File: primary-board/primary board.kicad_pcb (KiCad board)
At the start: 4 copper layers, 92 x 82 mm, 37 parts, among them J1 USB_C, J2 Sensor_Forward, J3 Sensor_Right, J4 Sensor_Left, J5 I2C Breakout, J6 Conn_01x02, J7 Conn_01x02, J8 Conn_01x02, SW1 SW_SPST, SW2 SW_SPST, U1 ESP32-S3-1, U2 L7806, U3 L7806, U4 AZ1117-3.3

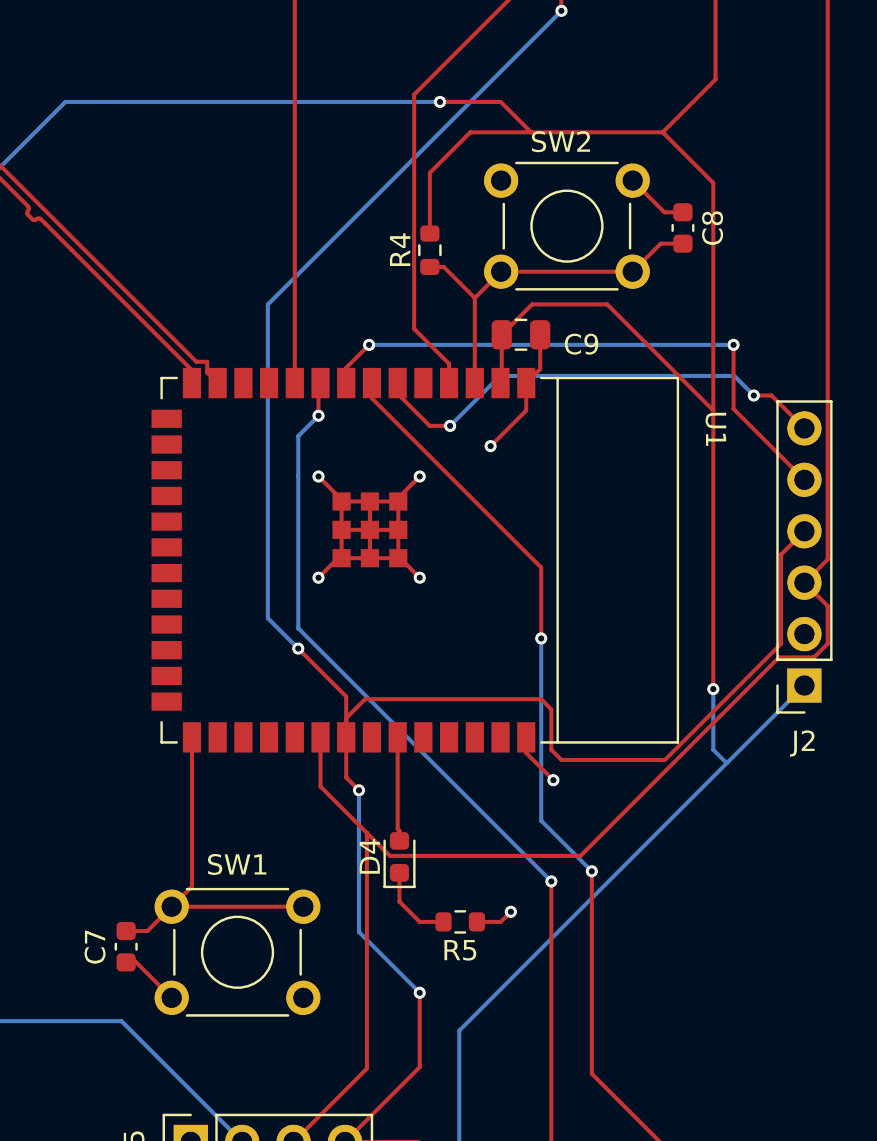
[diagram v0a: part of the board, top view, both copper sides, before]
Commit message: reorganized file tree swapped pushbuttons to smd
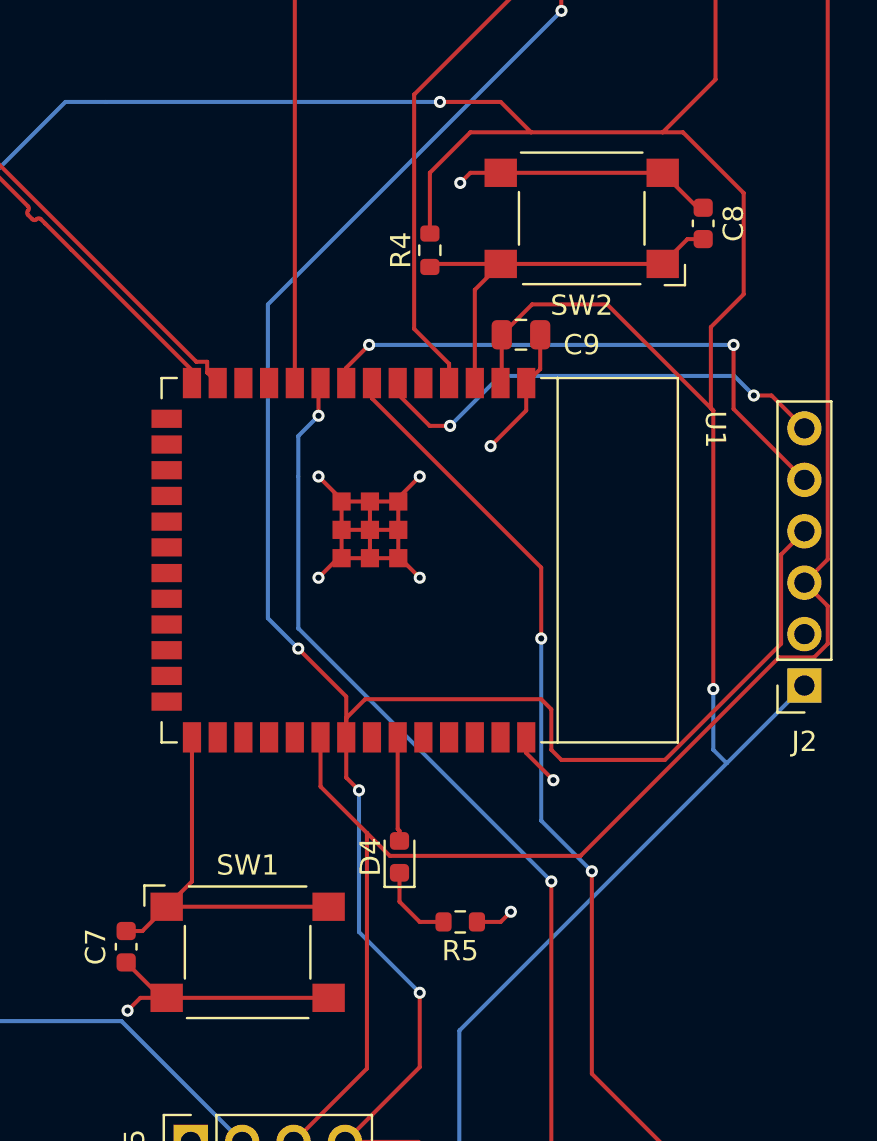
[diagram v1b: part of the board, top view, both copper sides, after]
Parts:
- SW1, SW2: footprint Button_Switch_THT:SW_TH_Tactile_Omron_B3F-100x -> Button_Switch_SMD:SW_SPST_Omron_B3FS-101xP
- moved SW1 4.37 mm to (163.0, 108.5)
- moved SW2 3.65 mm to (179.5, 72.2)
- moved C8 1.02 mm to (185.5, 72.5)
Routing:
- net GND: track 95.8 -> 115.5 mm, vias 21 -> 23
- net /MCU_ENABLE: track 18.4 -> 20.5 mm
- net +3.3V: track 267.5 -> 269.5 mm
- net /BOOT_SEL: track 18.0 -> 19.4 mm

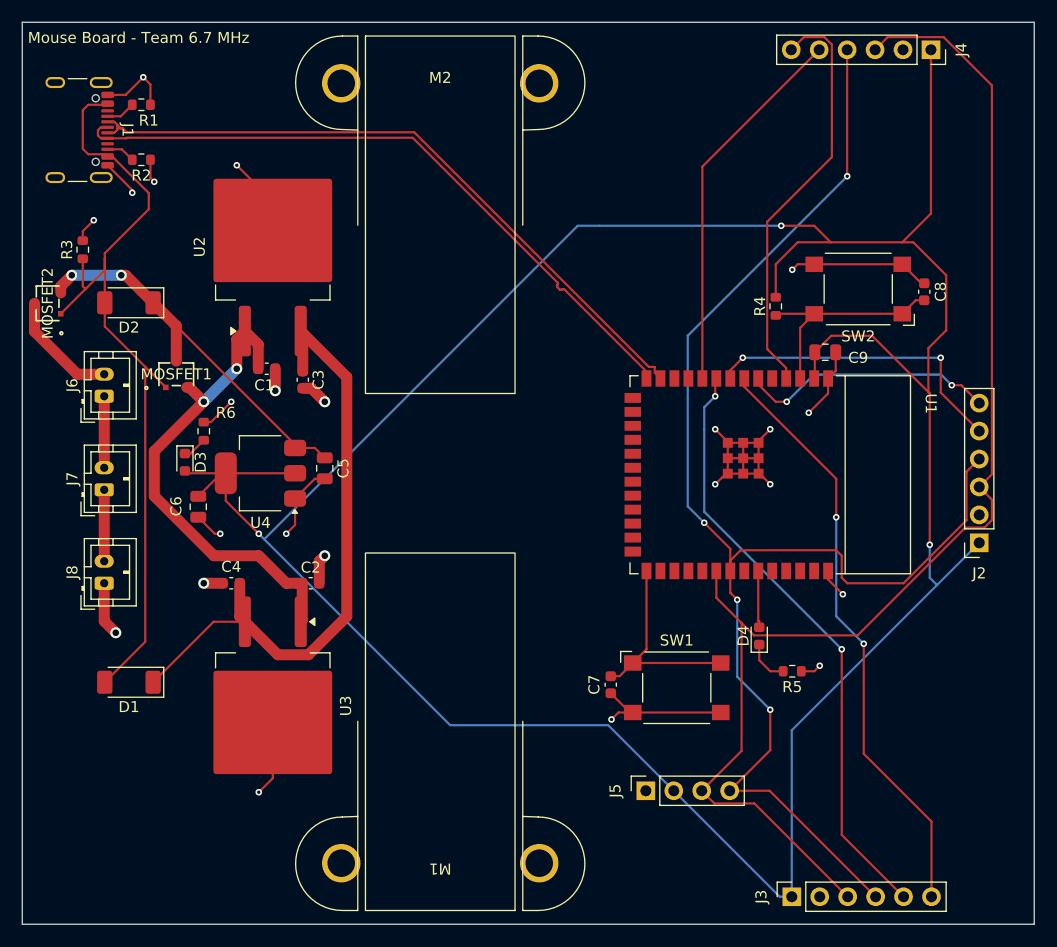
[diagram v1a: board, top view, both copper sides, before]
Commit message: added motor connectors and h-bridge
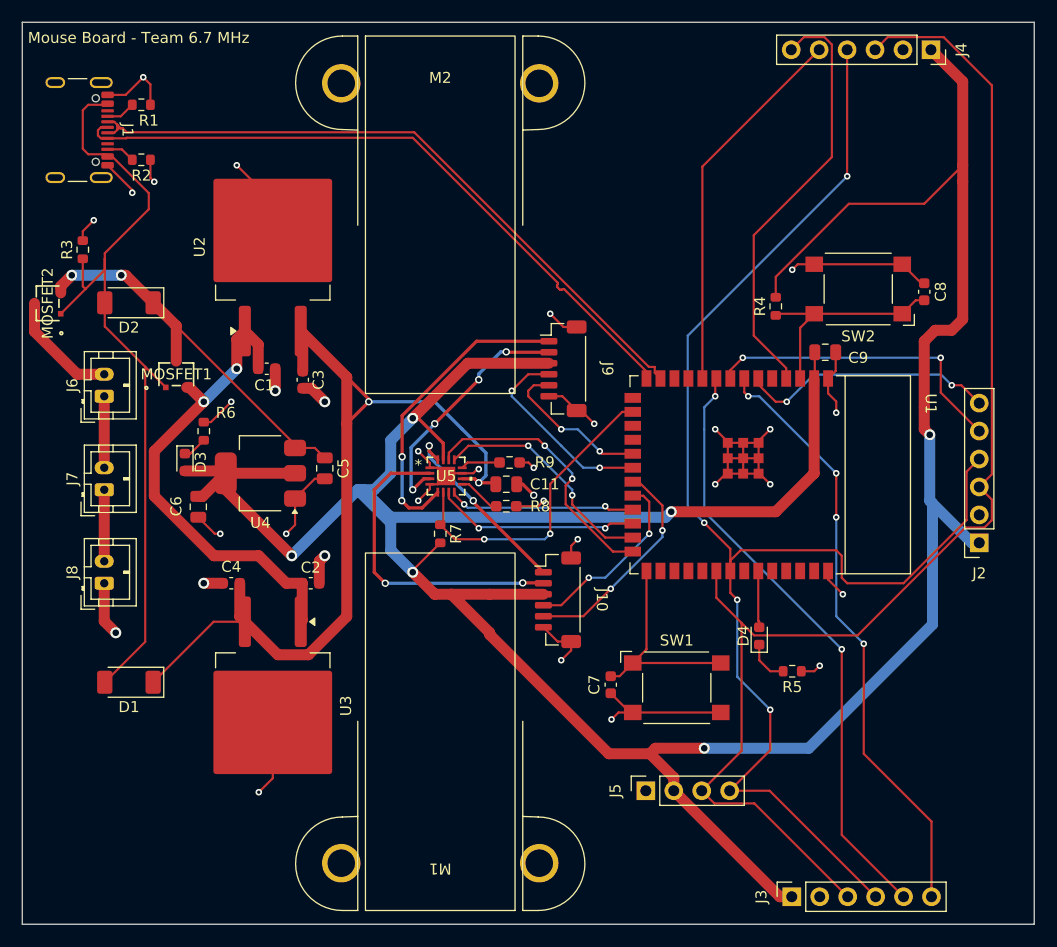
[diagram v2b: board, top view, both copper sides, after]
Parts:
- added C11: 22u, Capacitor_SMD:C_0805_2012Metric, F.Cu at (147.5, 90.0)
- added J10: Motor Connector Right, mouseLib:JST_SH_6_V, F.Cu at (152.5, 100.5)
- added J9: Motor Connector Left, mouseLib:JST_SH_6_V, F.Cu at (153.0, 79.5)
- added R7: 10k, Resistor_SMD:R_0603_1608Metric, F.Cu at (141.5, 94.5)
- added R8: 33k, Resistor_SMD:R_0603_1608Metric_Pad0.98x0.95mm_HandSolder, F.Cu at (147.5, 92.0)
- added R9: 33k, Resistor_SMD:R_0603_1608Metric_Pad0.98x0.95mm_HandSolder, F.Cu at (147.8, 88.0)
- added U5: DRV8411ARTER, drv8411:WQFN16_RTE_TEX, F.Cu at (142.0, 89.2)
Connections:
- U1 pad 16: unconnected-(U1-IO46-Pad16) -> /FAULT_HBRIDGE
- U1 pad 19: unconnected-(U1-IO11-Pad19) -> /ENC_B_LEFT
- U1 pad 20: unconnected-(U1-IO12-Pad20) -> /ENC_A_LEFT
- U1 pad 21: unconnected-(U1-IO13-Pad21) -> /ENC_B_RIGHT
- U1 pad 22: unconnected-(U1-IO14-Pad22) -> /ENC_A_RIGHT
- U1 pad 23: unconnected-(U1-IO21-Pad23) -> /PWM_LEFT_2
- U1 pad 24: unconnected-(U1-IO47-Pad24) -> /PWM_LEFT_1
- U1 pad 25: unconnected-(U1-IO48-Pad25) -> /PWM_RIGHT_2
- U1 pad 26: unconnected-(U1-IO45-Pad26) -> /PWM_RIGHT_1
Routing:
- net +3.3V: track 269.5 -> 301.4 mm, vias 3 -> 6
- net GND: track 115.5 -> 147.0 mm, vias 23 -> 33
- net /M2_RIGHT: track 0.00 -> 29.0 mm, vias 0 -> 2
- net /FAULT_HBRIDGE: track 0.00 -> 28.6 mm, vias 0 -> 2
- net /M1_LEFT: track 0.00 -> 28.0 mm, vias 0 -> 2
- net +6V: track 57.7 -> 82.4 mm, vias 0 -> 2
- net /PWM_RIGHT_1: track 0.00 -> 24.6 mm, vias 0 -> 2
- net /M2_LEFT: track 0.00 -> 22.3 mm, vias 0 -> 4
- net /PWM_RIGHT_2: track 0.00 -> 21.0 mm, vias 0 -> 2
- net /ENC_B_RIGHT: track 0.00 -> 20.3 mm, vias 0 -> 2
- net /PWM_LEFT_1: track 0.00 -> 18.7 mm, vias 0 -> 2
- net /ENC_A_LEFT: track 0.00 -> 18.2 mm, vias 0 -> 2
- net /M1_RIGHT: track 0.00 -> 17.4 mm, vias 0 -> 2
- net /PWM_LEFT_2: track 0.00 -> 17.1 mm, vias 0 -> 2
- net /ENC_A_RIGHT: track 0.00 -> 17.0 mm, vias 0 -> 2
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
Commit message: complete board reroute. changed drv fault line into mcu. thickened all traces
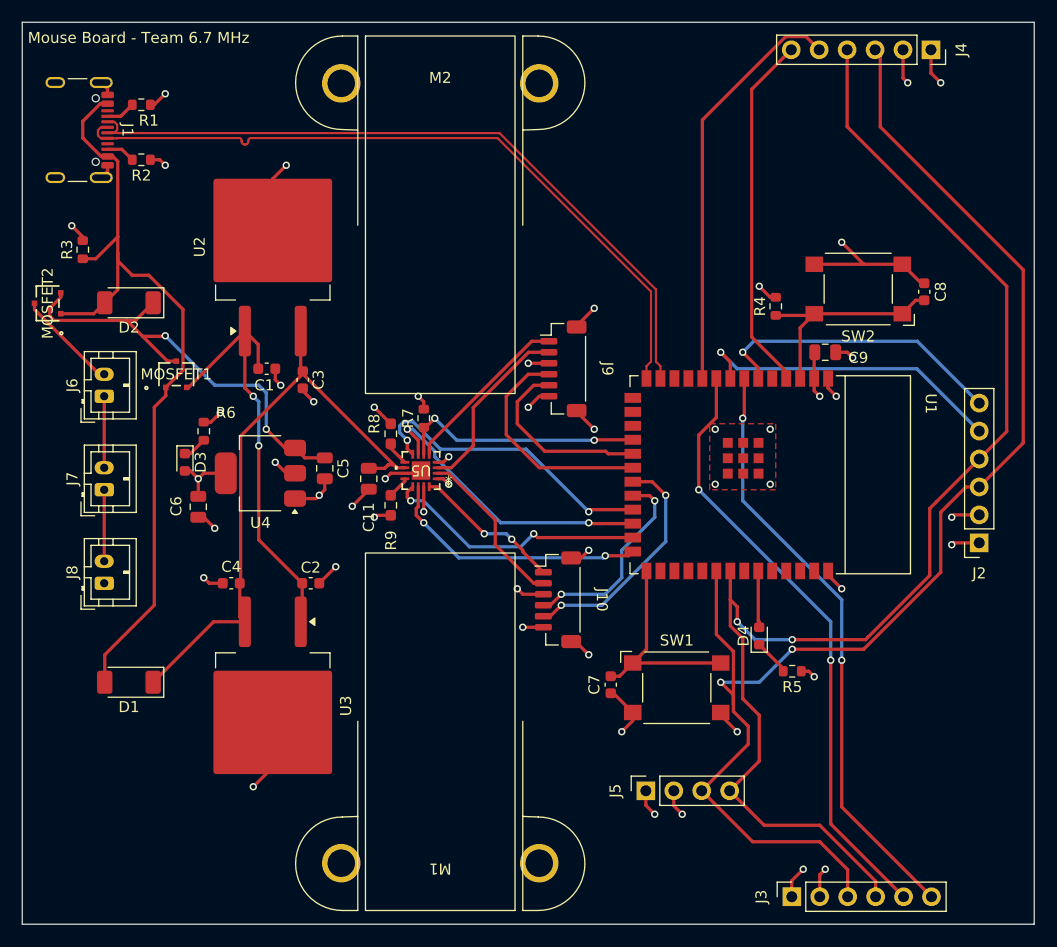
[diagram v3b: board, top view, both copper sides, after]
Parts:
- moved C11 12.5 mm to (135.0, 89.5), turned to -90 degrees
- moved R8 12.4 mm to (137.0, 85.4), turned to 90 degrees
- moved R9 11.5 mm to (137.0, 91.9), turned to -90 degrees
- moved R7 10.6 mm to (140.0, 84.0), turned to 90 degrees
- moved U5 2.33 mm to (139.7, 88.8), turned to 180 degrees
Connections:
- U1 pad 16: /FAULT_HBRIDGE -> unconnected-(U1-IO46-Pad16)
- U1 pad 18: unconnected-(U1-IO10-Pad18) -> /FAULT_HBRIDGE
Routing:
- net +3.3V: track 301.4 -> 33.6 mm, vias 6 -> 12
- net GND: track 147.0 -> 99.6 mm, vias 33 -> 39
- net +6V: track 82.4 -> 55.1 mm, vias 2 -> 0
- net /M2_RIGHT: track 29.0 -> 15.1 mm, vias 2 -> 0
- net /M1_LEFT: track 28.0 -> 15.7 mm, vias 2 -> 0
- net /PWM_LEFT_2: track 17.1 -> 27.9 mm
- net /MCU_SDA: track 128.9 -> 119.8 mm, vias 4 -> 2
- net /PWM_LEFT_1: track 18.7 -> 27.0 mm
- net /LEFT_SHUTDOWN: track 39.0 -> 32.7 mm
- net /FAULT_HBRIDGE: track 28.6 -> 22.6 mm
- net /M2_LEFT: track 22.3 -> 16.5 mm, vias 4 -> 0
- net /USB_D+: track 61.2 -> 66.4 mm
- net Net-(U2-IN): track 44.7 -> 40.0 mm
- net /MCU_SCL: track 120.6 -> 125.1 mm, vias 0 -> 2
- net /USB_D-: track 62.1 -> 66.5 mm
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- added copper zone on In2.Cu, net +3.3V
- added copper zone on F.Cu, net GND
